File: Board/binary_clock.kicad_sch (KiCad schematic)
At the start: 0 parts

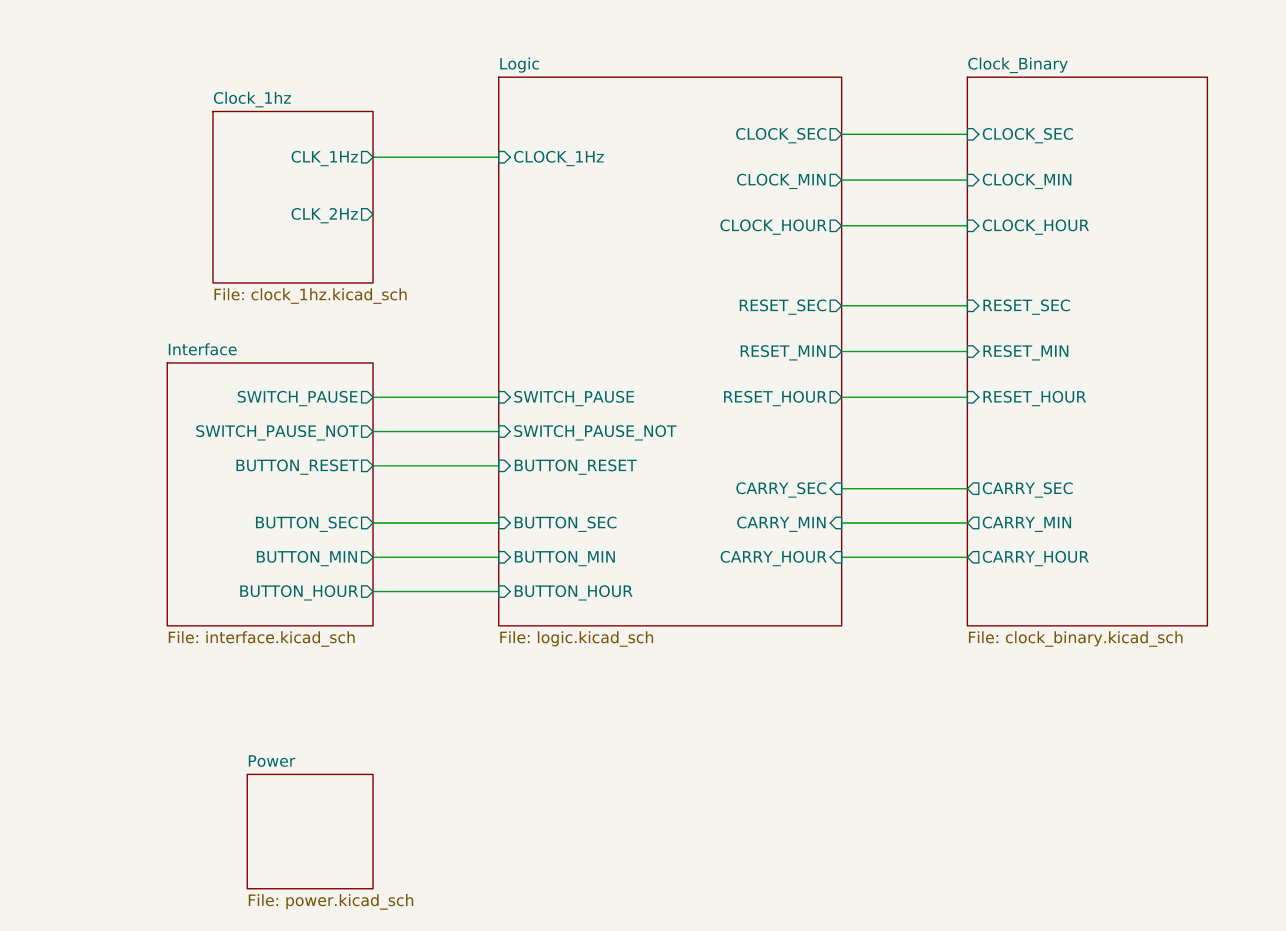
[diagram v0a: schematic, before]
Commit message: make power circuit from 120v mains
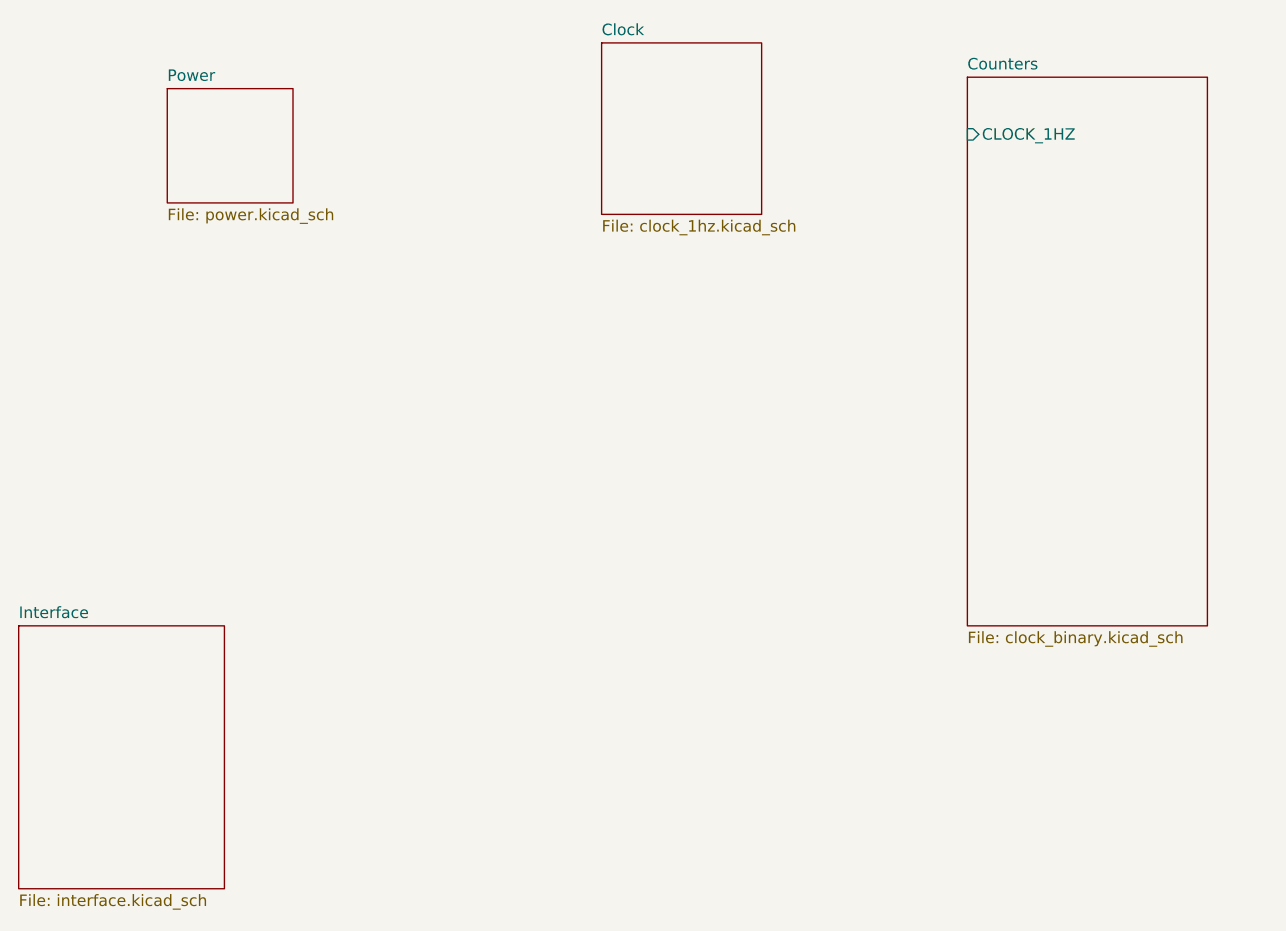
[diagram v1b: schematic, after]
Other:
- sheet Clock_1hz renamed Clock
- sheet Clock_Binary renamed Counters
- removed sheet Logic
- sheet Clock ports: added none; removed CLK_1Hz, CLK_2Hz
- sheet Counters ports: added CLOCK_1HZ; removed CARRY_HOUR, CARRY_MIN, CARRY_SEC, CLOCK_HOUR, CLOCK_MIN, CLOCK_SEC, RESET_HOUR, RESET_MIN, RESET_SEC
- sheet Interface ports: added none; removed BUTTON_HOUR, BUTTON_MIN, BUTTON_RESET, BUTTON_SEC, SWITCH_PAUSE, SWITCH_PAUSE_NOT

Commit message: start work on clock
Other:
- sheet Clock ports: added AC_SENSE, CLOCK_1HZ; removed none
- sheet Power ports: added AC_SENSE; removed none
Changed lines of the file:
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@@
 	(generator_version "9.0")
 	(paper "A5")
+	(wire
+		(pts
+			(xy 76.2 40.64) (xy 90.17 40.64)
+		)
+		(stroke
+			(width 0)
+			(type default)
+		)
+	)
+	(wire
+		(pts
+			(xy 50.8 35.56) (xy 62.23 35.56)
+		)
+		(stroke
+			(width 0)
+			(type default)
+		)
+	)
 	(sheet
-		(at 137.16 31.75)
+		(at 90.17 31.75)
 		(size 26.67 60.96)
 		(exclude_from_sim no)
@@
 		)
 		(property "Sheetname" "Counters"
-			(at 137.16 31.0384 0)
+			(at 90.17 31.0384 0)
 			(effects
 				(font
@@
 		)
 		(property "Sheetfile" "clock_binary.kicad_sch"
-			(at 137.16 93.2946 0)
+			(at 90.17 93.2946 0)
 			(effects
 				(font
@@
 		)
 		(pin "CLOCK_1HZ" input
-			(at 137.16 38.1 180)
+			(at 90.17 40.64 180)
 			(effects
 				(font
@@
 	)
 	(sheet
-		(at 48.26 33.02)
+		(at 36.83 31.75)
 		(size 13.97 12.7)
 		(exclude_from_sim no)
@@
 		)
 		(property "Sheetname" "Power"
-			(at 48.26 32.3084 0)
+			(at 36.83 31.0384 0)
 			(effects
 				(font
@@
 		)
 		(property "Sheetfile" "power.kicad_sch"
-			(at 48.26 46.3046 0)
+			(at 36.83 45.0346 0)
 			(effects
 				(font
@@
 				)
 				(justify left top)
+			)
+		)
+		(pin "AC_SENSE" output
+			(at 50.8 35.56 0)
+			(effects
+				(font
+					(size 1.27 1.27)
+				)
+				(justify right)
 			)
 		)
@@
 	)
 	(sheet
-		(at 96.52 27.94)
-		(size 17.78 19.05)
+		(at 62.23 31.75)
+		(size 13.97 12.7)
 		(exclude_from_sim no)
 		(in_bom yes)
@@
 		)
 		(property "Sheetname" "Clock"
-			(at 96.52 27.2284 0)
+			(at 62.23 31.0384 0)
 			(effects
 				(font
@@
 		)
 		(property "Sheetfile" "clock_1hz.kicad_sch"
-			(at 96.52 47.5746 0)
+			(at 62.23 45.0346 0)
 			(effects
 				(font
@@
 			)
 		)
+		(pin "AC_SENSE" input
+			(at 62.23 35.56 180)
+			(effects
+				(font
+					(size 1.27 1.27)
+				)
+				(justify left)
+			)
+		)
+		(pin "CLOCK_1HZ" output
+			(at 76.2 40.64 0)
+			(effects
+				(font
+					(size 1.27 1.27)
+				)
+				(justify right)
+			)
+		)
